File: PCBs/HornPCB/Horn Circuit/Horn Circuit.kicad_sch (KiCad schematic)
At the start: 19 parts, among them J1 Screw_Terminal_01x02 Speaker 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, J2 2301844-1, J4 2301844-1, U1 ESP32-S3-DevKitC, U2 DFR0299, U3 SN65HVD230DR

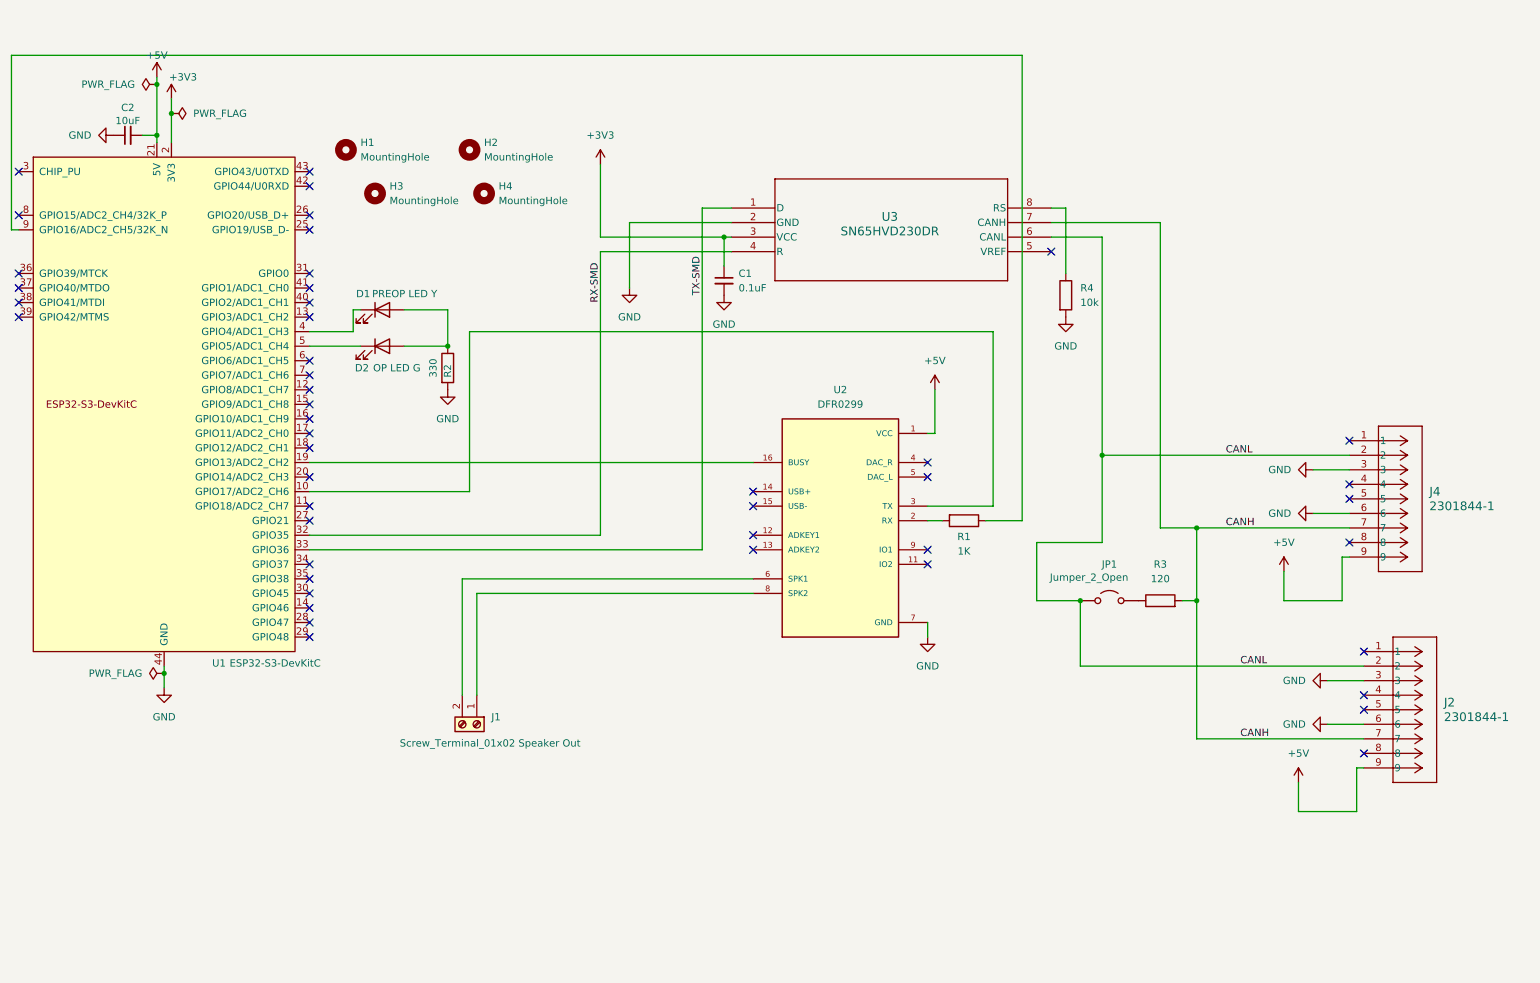
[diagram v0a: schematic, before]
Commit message: Updated kicad project files for horn
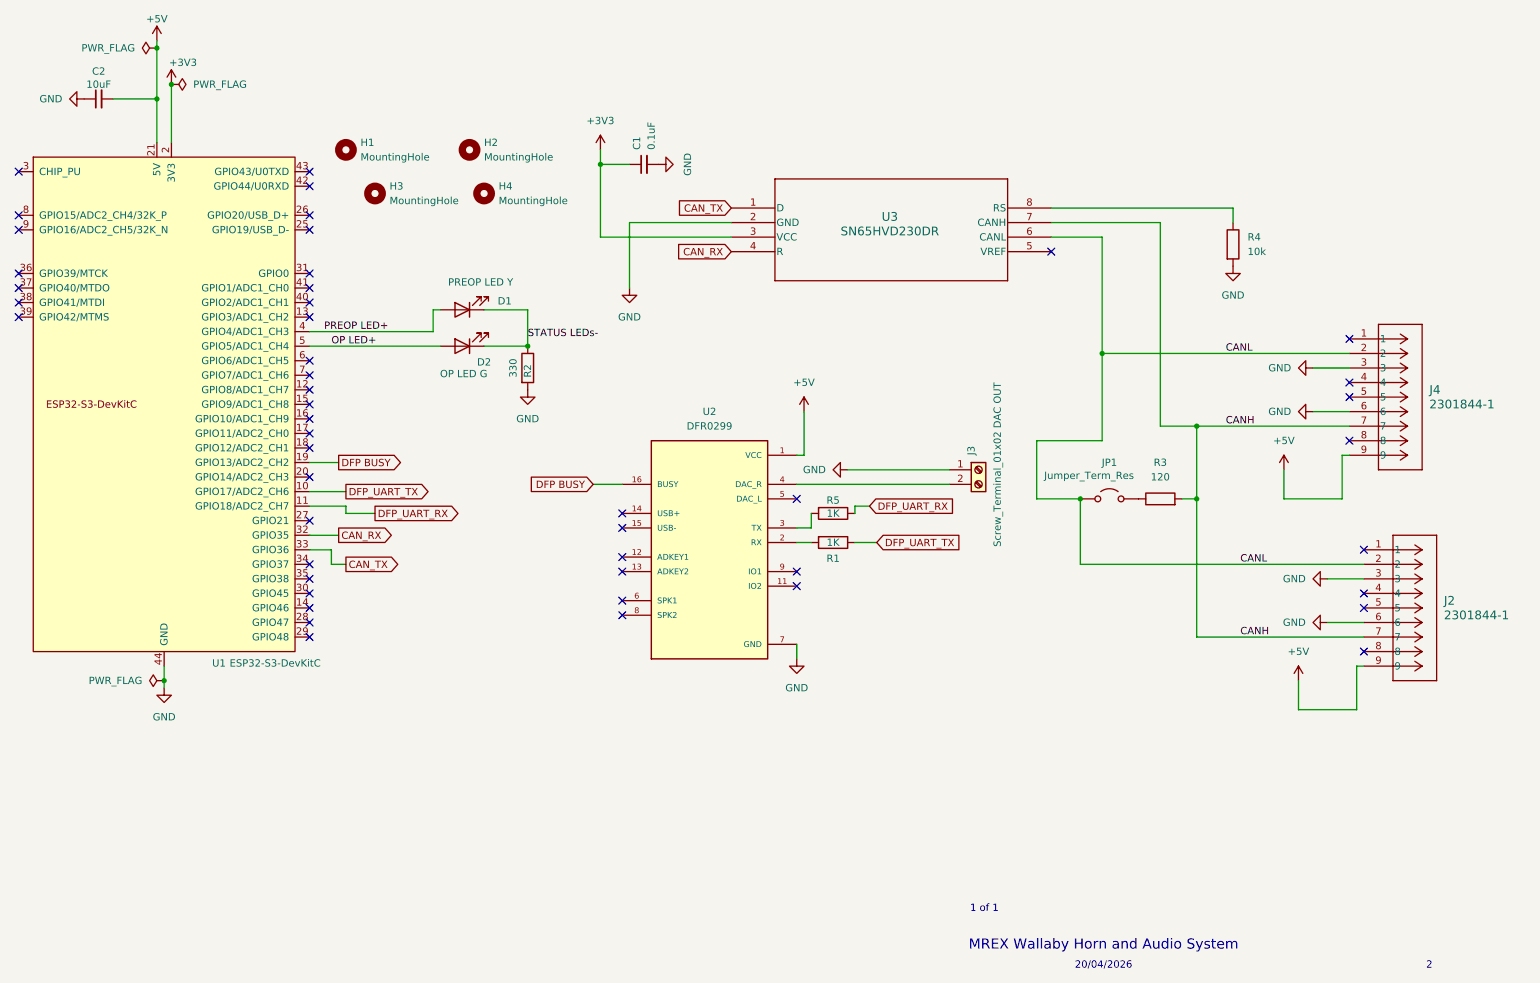
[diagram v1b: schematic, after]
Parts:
- removed J1: Screw_Terminal_01x02 Speaker Out, TerminalBlock_4Ucon:TerminalBlock_4Ucon_1x02_P3.50mm_Horizontal, symbol Connector:Screw_Terminal_01x02
- added J3: Screw_Terminal_01x02 DAC OUT, TerminalBlock_Phoenix:TerminalBlock_Phoenix_MKDS-1,5-2-5.08_1x02_P5.08mm_Horizontal, symbol Connector:Screw_Terminal_01x02
- added R5: 1K, Resistor_THT:R_Axial_DIN0207_L6.3mm_D2.5mm_P7.62mm_Horizontal, symbol Device:R
- JP1: value Jumper_2_Open -> Jumper_Term_Res
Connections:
- net GND: now also J3.1 (Pin_1)
- net at U2.3 (TX): now also R5.2; no longer U1.10 (GPIO17/ADC2_CH6)
- net DFP_UART_RX: now reaches U1.11 (GPIO18/ADC2_CH7)
- net DFP_UART_RX: now also R5.1
- net DFP BUSY: now reaches U1.19 (GPIO13/ADC2_CH2), U2.16 (BUSY)
- net PREOP LED+: now reaches U1.4 (GPIO4/ADC1_CH3)
- net PREOP LED+: now also D1.2 (A); no longer D1.1 (K)
- net OP LED+: now reaches U1.5 (GPIO5/ADC1_CH4)
- net OP LED+: now also D2.2 (A); no longer D2.1 (K)
- net at U1.9 (GPIO16/ADC2_CH5/32K_N): no longer R1.1
- net at U2.4 (DAC_R): now also J3.2 (Pin_2)
- net RX-SMD renamed CAN_RX
- net TX-SMD renamed CAN_TX
- new net DFP_UART_TX: R1.1, U1.10 (GPIO17/ADC2_CH6)
- new net STATUS LEDs-: D1.1 (K), D2.1 (K), R2.1
- no-connect marks 47 -> 48
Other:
- note added: "1 of 1"
- note added: "2"
- note added: "20/04/2026"
- note added: "MREX Wallaby Horn and Audio System"
- moved on the sheet: C1, C2, D1, D2, J2, J4, JP1, R1, R2, R3, R4, U2

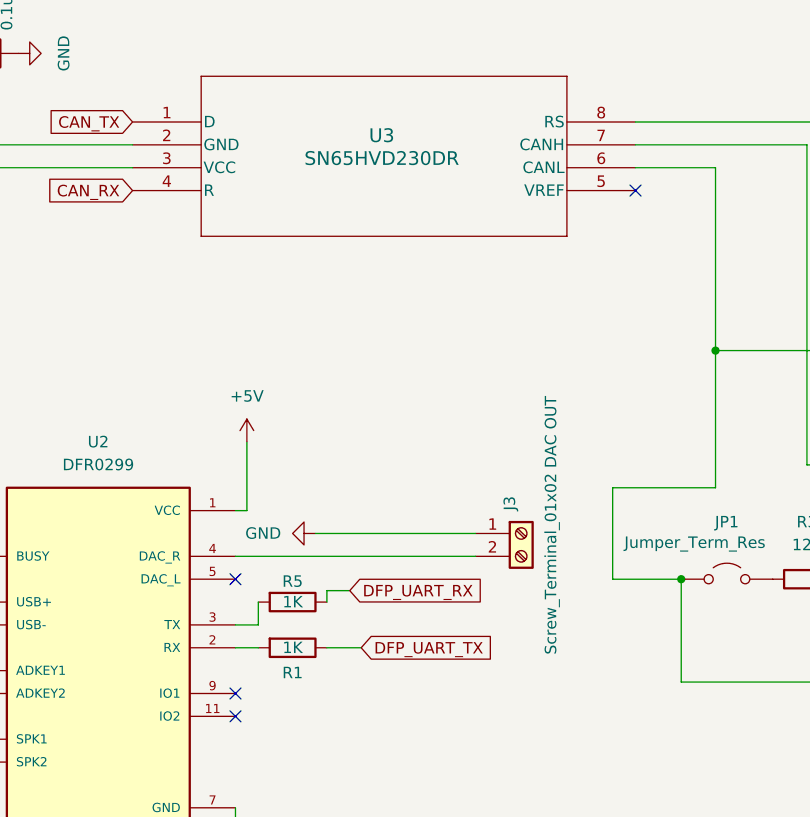
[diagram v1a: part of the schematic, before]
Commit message: DFPlayer DAC_R outputs
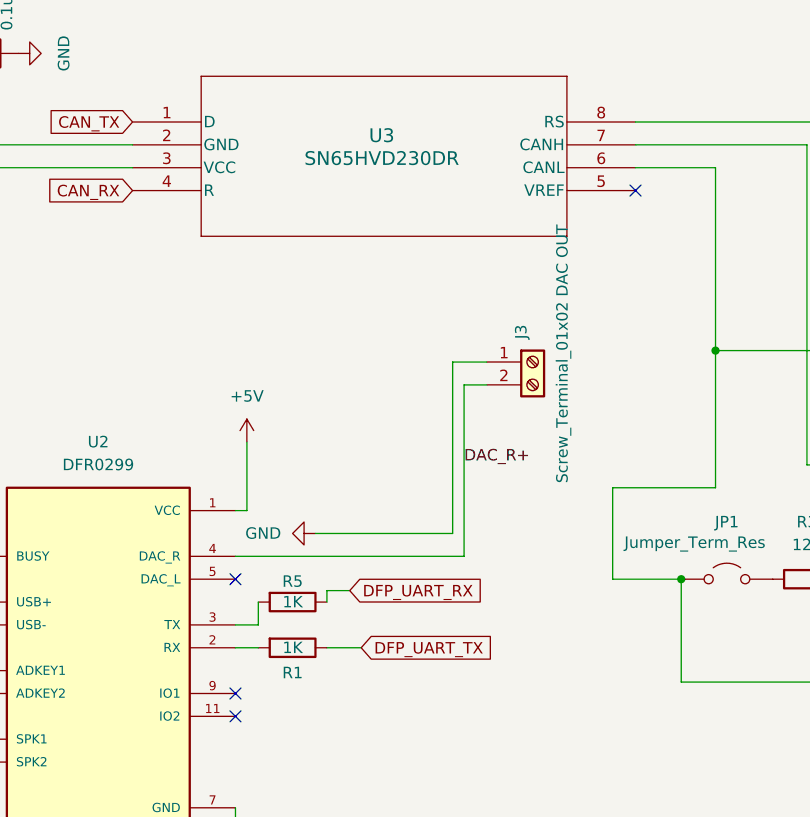
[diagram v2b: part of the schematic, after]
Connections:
- net DAC_R+: now reaches J3.2 (Pin_2), U2.4 (DAC_R)
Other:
- moved on the sheet: J3
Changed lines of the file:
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@@
 	(wire
 		(pts
-			(xy 167.64 106.68) (xy 185.42 106.68)
+			(xy 182.88 87.63) (xy 186.69 87.63)
 		)
 		(stroke
@@
 	(wire
 		(pts
+			(xy 184.15 109.22) (xy 158.75 109.22)
+		)
+		(stroke
+			(width 0)
+			(type default)
+		)
+	)
+	(wire
+		(pts
 			(xy 77.47 123.19) (xy 80.01 123.19)
 		)
@@
 	(wire
 		(pts
-			(xy 158.75 109.22) (xy 185.42 109.22)
+			(xy 184.15 90.17) (xy 186.69 90.17)
 		)
 		(stroke
@@
 	(wire
 		(pts
+			(xy 182.88 87.63) (xy 182.88 106.68)
+		)
+		(stroke
+			(width 0)
+			(type default)
+		)
+	)
+	(wire
+		(pts
 			(xy 212.09 66.04) (xy 212.09 86.36)
 		)
@@
 	(wire
 		(pts
+			(xy 184.15 90.17) (xy 184.15 109.22)
+		)
+		(stroke
+			(width 0)
+			(type default)
+		)
+	)
+	(wire
+		(pts
 			(xy 46.99 41.91) (xy 46.99 49.53)
 		)
@@
 		(pts
 			(xy 243.84 106.68) (xy 243.84 111.76)
+		)
+		(stroke
+			(width 0)
+			(type default)
+		)
+	)
+	(wire
+		(pts
+			(xy 182.88 106.68) (xy 167.64 106.68)
 		)
 		(stroke
@@
 	(label "OP LED+"
 		(at 77.47 85.09 0)
+		(effects
+			(font
+				(size 1.27 1.27)
+			)
+			(justify left bottom)
+		)
+	)
+	(label "DAC_R+"
+		(at 184.15 99.06 0)
 		(effects
 			(font
@@
 	(symbol
 		(lib_id "Connector:Screw_Terminal_01x02")
-		(at 190.5 106.68 0)
+		(at 191.77 87.63 0)
 		(unit 1)
 		(exclude_from_sim no)
@@
 		(dnp no)
 		(property "Reference" "J3"
-			(at 189.2299 104.14 90)
+			(at 190.4999 85.09 90)
 			(effects
 				(font
@@
 		)
 		(property "Value" "Screw_Terminal_01x02 DAC OUT"
-			(at 193.802 120.142 90)
+			(at 195.072 101.092 90)
 			(effects
 				(font
@@
 		)
 		(property "Footprint" "TerminalBlock_Phoenix:TerminalBlock_Phoenix_MKDS-1,5-2-5.08_1x02_P5.08mm_Horizontal"
-			(at 190.5 106.68 0)
+			(at 191.77 87.63 0)
 			(effects
 				(font
@@
 		)
 		(property "Datasheet" "~"
-			(at 190.5 106.68 0)
+			(at 191.77 87.63 0)
 			(effects
 				(font
@@
 		)
 		(property "Description" "Generic screw terminal, single row, 01x02, script generated (kicad-library-utils/schlib/autogen/connector/)"
-			(at 190.5 106.68 0)
-			(effects
-				(font
+			(at 191.77 87.63 0)
+			(effects
+				(font
